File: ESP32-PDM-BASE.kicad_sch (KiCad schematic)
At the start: 13 parts, among them J1 Conn_02x06_Top_Bottom, U1 ESP32-S3-MINI-1

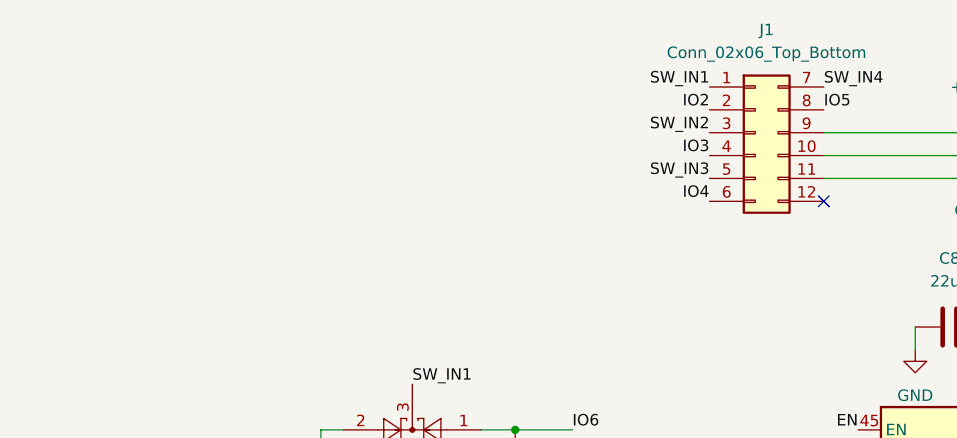
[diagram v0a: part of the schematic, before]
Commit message: Fix LED driver bias, add ST pull-ups, name TPS7B91 NC pins
- Swap LED driver base resistors: 2.2k series (R18/R20/R23/R26) and
  10k pull-down (R17/R21/R24/R27). The old 10k/2.2k divider only gave
  ~0.6 V at the base, so the NPNs never turned on.
- Add 10k pull-ups R29-R32 from IO2-IO5 to +3V3 for the open-drain ST
  outputs of the TPS1H100-Q1 switches on the output module.
- Name TPS7B91 pins 3 and 4 "NC" (datasheet: not internally connected).

ERC violation count unchanged (45, all pre-existing).

Co-Authored-By: Claude Opus 5.5 <noreply@anthropic.com>
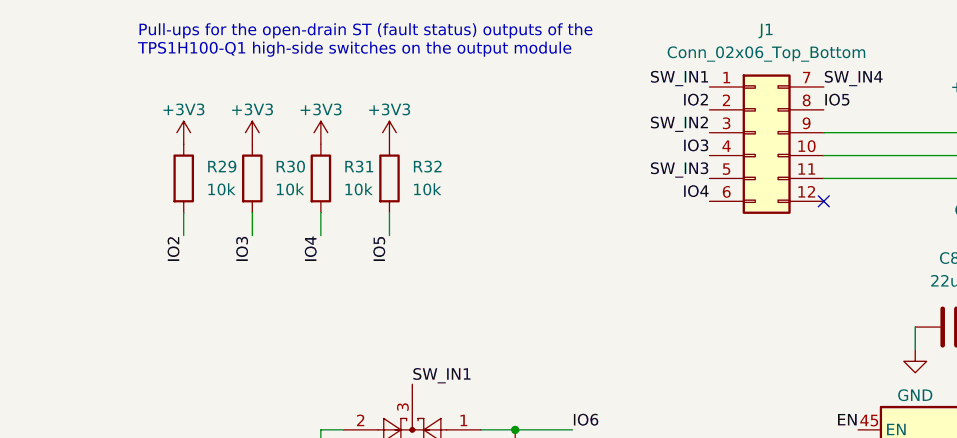
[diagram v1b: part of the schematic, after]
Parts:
- added R29, R30, R31, R32: 10k, Resistor_SMD:R_0402_1005Metric, symbol Device:R
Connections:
- net +3V3: now also R29.1, R30.1, R31.1, R32.1
- net IO2: now also R29.2
- net IO3: now also R30.2
- net IO4: now also R31.2
- net IO5: now also R32.2
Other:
- note added: "Pull-ups for the open-drain ST (fault status) outputs of the TPS1H100-Q1 high-side switches on the output module"

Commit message: Apply JLCPCB BOM audit fixes and add module ID / switch sense
- Remove CH340C and auto-reset circuit; USB-C goes to native USB
  (IO19 = D-, IO20 = D+). UART0 left unconnected.
- USB-C: HRO TYPE-C-31-M-12 (shell pins renumbered SH to match footprint).
- F1/F3: 1812L050/60GR (60 V, 500 mA hold); old part was rated 30 V max.
- D2/D3/D11: DSK16 (60 V) replacing out-of-stock DSS14U.
- D9: PESD2CAN replacing unavailable ESDCAN01-2BWY (SOT-23).
- L1: SWPA6045S8R2MT (Isat 3.9 A > LMR51610 peak limit 1.95 A).
- Feedback divider 68k/22k (basic parts): Vout 3.27 V with Vref 0.8 V.
- Basic-library swaps: TS-1187A buttons, 0805 2.2uF/50V, 49.9 R,
  BC817-40.
- Move the ST pull-ups to the output module.
- Header pin 12 becomes MOD_ID (IO1, 10k pull-up).
- SW1-SW4 to IO14/IO15/IO16/IO21 with 10k pull-downs, so the firmware
  can read the physical switches.
- Add LCSC part numbers for changed parts and main ICs.

ERC: 38 violations (was 45), none new except a missing PWR_FLAG on
+3V3 now that the CH340C no longer drives it.

Co-Authored-By: Claude Opus 5.5 <noreply@anthropic.com>
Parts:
- added R33: 10k, Resistor_SMD:R_0402_1005Metric, symbol Device:R
- R29, R30, R31, R32: LCSC (none) -> C25744
- U1: LCSC (none) -> C2913206
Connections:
- net Analog interface/SW1 is gone; now on net SW1: D12.2
- net Analog interface/SW2 is gone; now on net SW2: D13.2
- net Analog interface/SW3 is gone; now on net SW3: D14.2
- net Analog interface/SW4 is gone; now on net SW4: D15.2
- net +3V3: no longer R30.1, R31.1, R32.1
- net GND: now also R30.2, R31.2, R32.2, R33.2
- net IO2: no longer R29.2
- net IO3: no longer R30.2
- net IO4: no longer R31.2
- net IO5: no longer R32.2
- net MOD_ID: now reaches J1.12 (Pin_12)
- net MOD_ID: now also R29.2, U1.5 (IO1)
- net SW1: now reaches U1.18 (IO14)
- net SW1: now also R30.1
- net SW2: now reaches U1.19 (IO15)
- net SW2: now also R31.1
- net SW3: now reaches U1.20 (IO16)
- net SW3: now also R32.1
- net USB_DN: now reaches U1.23 (IO19)
- net USB_DP: now reaches U1.24 (IO20)
- net SW4: now reaches U1.25 (IO21)
- net SW4: now also R33.1
- net USB_RXD: no longer names the net of U1.39 (TXD0)
- net USB_TXD: no longer names the net of U1.40 (RXD0)
- no-connect marks 1 -> 2
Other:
- sheet Power and USB ports: added USB_DN, USB_DP; removed RXD, TXD
- note added: "MOD_ID: module pulls header pin 12 down (0 V = 4x4 rev 1); read on IO1 (ADC). SW1-SW4: physical switch state for the firmware (opto outputs, 10k pull-downs)."
- note removed: "Pull-ups for the open-drain ST (fault status) outputs of the TPS1H100-Q1 high-side switches on the output module"

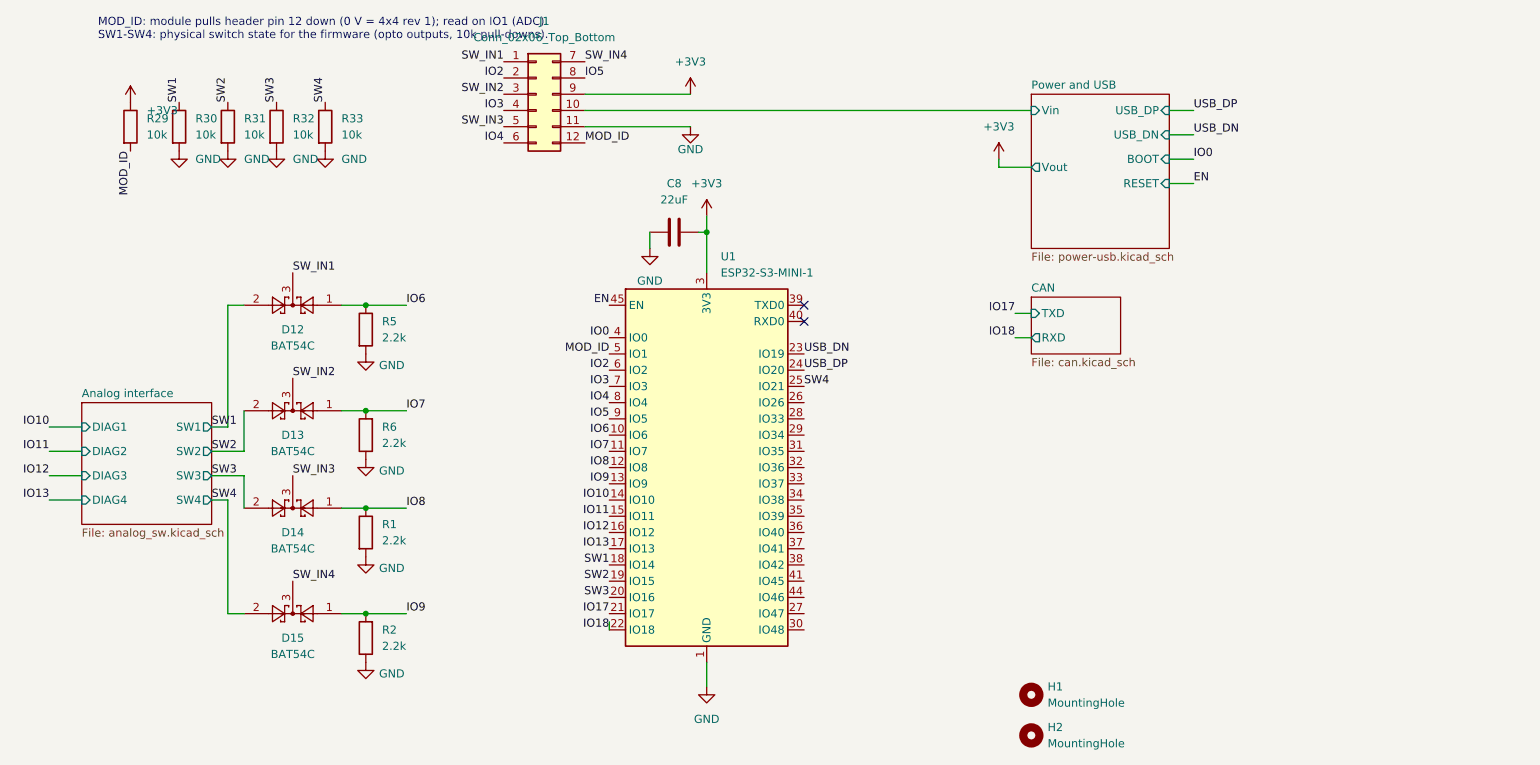
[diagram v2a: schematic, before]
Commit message: Harden inputs for 30 V, finish BOM swaps, clean up ERC
- Switch inputs R3/R4/R7/R8: 330 R -> 4.7k 1206. 2 mA at 10.5 V,
  6.1 mA / 0.18 W at 30 V. LTV-247 CTR >= 50 % at 5 mA, ~0.7x at 2 mA
  (datasheet fig. 10) -> >= 0.7 mA out vs 0.33 mA needed.
- D1: SMAJ30CA (clamp 48.4 V, below the 50 V input caps).
- D10: SMAJ18CA on NMEA 2000 NET-S (9-16 V); clamp 29.2 V protects the
  TPS7B91 (42 V abs max). SMAJ33CA clamped at 53 V.
- F2: SMD0805B050TF; D4-D6: PESD0402V05; J4: WJ15EDGVC-3.81-04P
  (MCV 1.5 clone, footprint kept - verify against datasheet).
- ERC: PWR_FLAGs on +3V3, GND, VBUS, buck VIN, CAN LDO input, GND_CAN;
  LMR51610 symbol CB/FB/SW pins passive; spare GPIOs no-connect;
  orphaned CH340 GND symbol and IO18 stub removed; LED_C stub wires
  trimmed to their labels.

Netlist connectivity identical to previous commit. ERC: 8 left, all
lib_symbol_mismatch (BC817, LTV-247) - use Update Symbols from Library.

Co-Authored-By: Claude Opus 5.5 <noreply@anthropic.com>
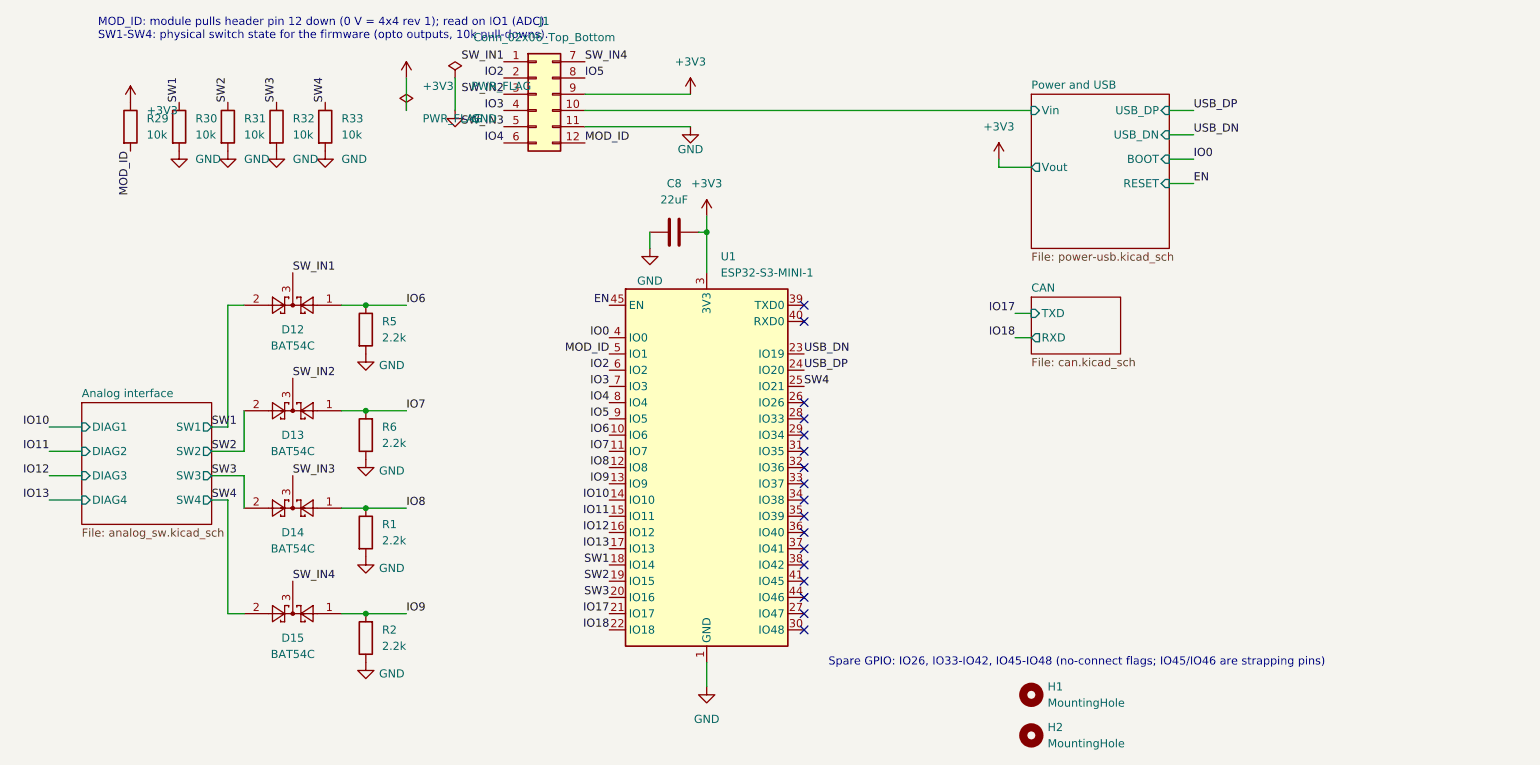
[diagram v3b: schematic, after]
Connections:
- no-connect marks 2 -> 17
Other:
- note added: "Spare GPIO: IO26, IO33-IO42, IO45-IO48 (no-connect flags; IO45/IO46 are strapping pins)"

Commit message: Replace opto switch inputs with protected direct inputs
The physical switch now drives the output EN without the LTV-247 and
without depending on the 3.3 V rail. Per input:
- SMAJ30CA TVS at J5 (surge/ESD on long switch cables)
- 4.7k 1206 load to GND (contact wetting 2.5 mA @ 12 V, 6.4 mA @ 30 V)
- 10k 1206 series + 4.7k/BZT52C3V3 divider-clamp + 100 nF:
  node ~3.2 V for 10.5-30 V in, EN threshold ~7.5 V, tau ~0.3 ms,
  negative spikes clamped by the Zener/TVS
- node -> existing BAT54C diode-OR -> SW_IN (module EN)
- R30-R33 now 10k series from the node to IO14/IO15/IO16/IO21,
  limiting back-feed into an unpowered ESP32 to ~0.3 mA

ERC: 4 left (BC817 lib_symbol_mismatch).

Co-Authored-By: Claude Opus 5.5 <noreply@anthropic.com>
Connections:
- net GND: no longer R30.2, R31.2, R32.2, R33.2
- net SW1: no longer U1.18 (IO14)
- net SW2: no longer U1.19 (IO15)
- net SW3: no longer U1.20 (IO16)
- net SW4: no longer U1.25 (IO21)
- new net SW1_IO: R30.2, U1.18 (IO14)
- new net SW2_IO: R31.2, U1.19 (IO15)
- new net SW3_IO: R32.2, U1.20 (IO16)
- new net SW4_IO: R33.2, U1.25 (IO21)
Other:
- note added: "MOD_ID: module pulls header pin 12 down (0 V = 4x4 rev 1); read on IO1 (ADC). SW1-SW4: switch state from the input dividers, 10k series to IO14/IO15/IO16/IO21."
- note removed: "MOD_ID: module pulls header pin 12 down (0 V = 4x4 rev 1); read on IO1 (ADC). SW1-SW4: physical switch state for the firmware (opto outputs, 10k pull-downs)."
